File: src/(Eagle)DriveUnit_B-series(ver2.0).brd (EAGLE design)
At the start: 65.7 x 51 mm, 68 parts, among them IC1 A3921, SW1 TVAF06-A020B-R, SW2 TVAF06-A020B-R, SW3 THAF01-NC-R, SW4 SS-12D00G3

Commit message: 配線の追加
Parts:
- removed R28: 100k, GF063P B104K:GF063PB104K
- moved R12 0.20 mm to (49.2, 31.0)
- moved R10 0.17 mm to (49.2, 28.6)
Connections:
- removed net N$16: R13.RIGHT, R28.CENTER, R28.RIGHT
- net GND: now also R13.RIGHT; no longer R28.LEFT
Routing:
- net N$16: track 20.5 -> 0.00 mm, vias 2 -> 0
- net V5: track 23.1 -> 28.3 mm
- net VCC: track 0.00 -> 3.87 mm, vias 0 -> 2
- net GLB: track 10.2 -> 11.4 mm
- net GHB: track 7.57 -> 6.62 mm
- net N$4: track 6.13 -> 5.42 mm

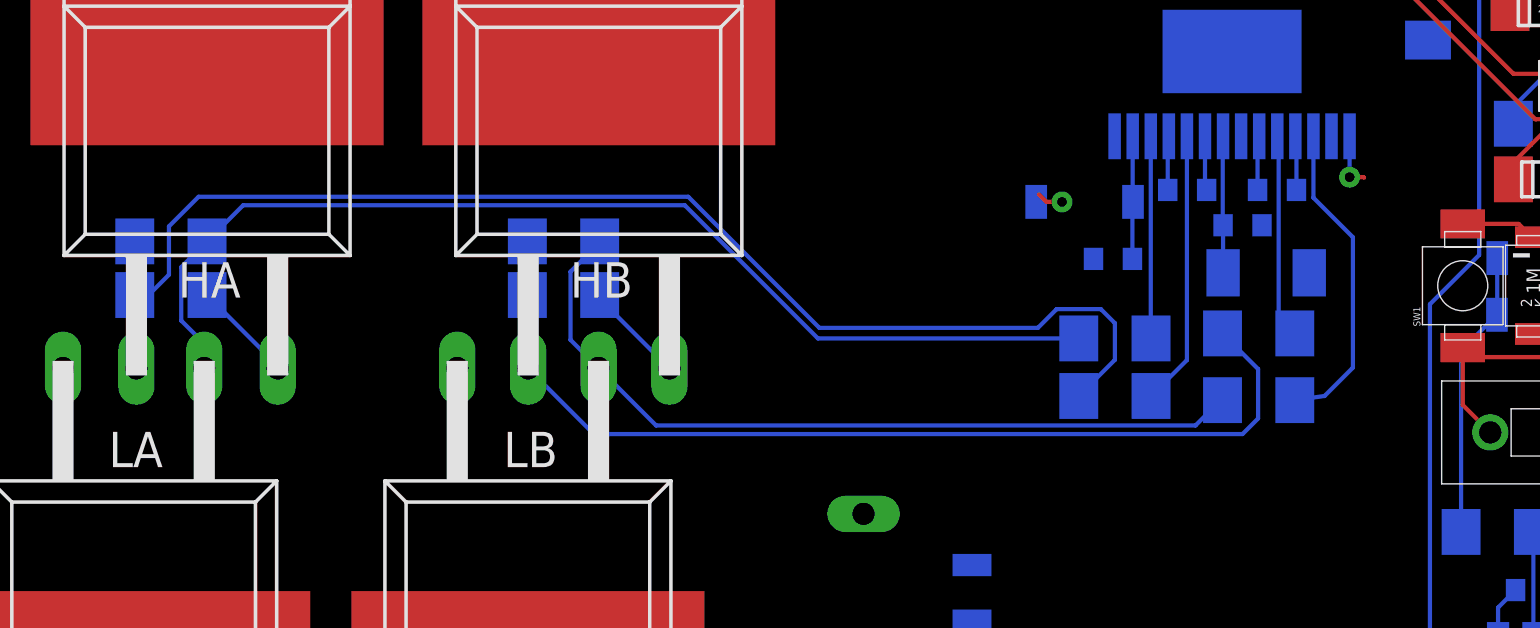
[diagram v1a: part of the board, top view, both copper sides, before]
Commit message: ビアなどの追加
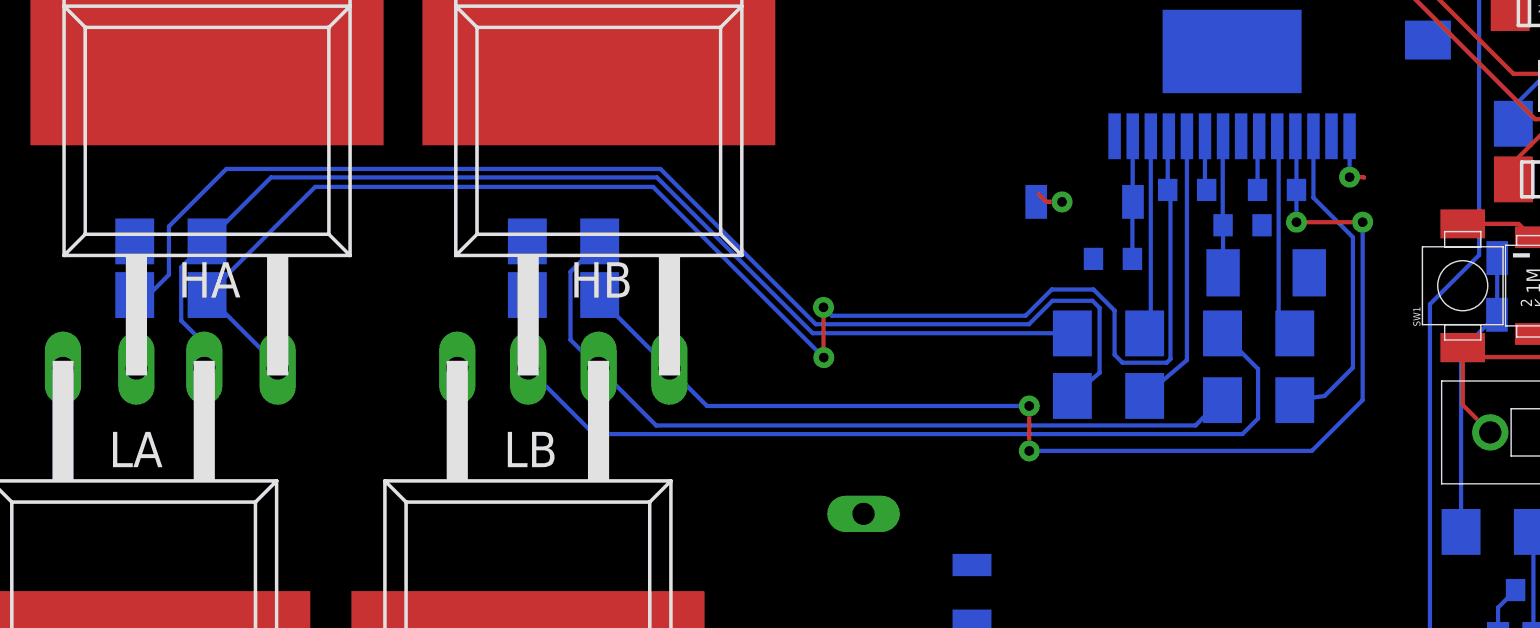
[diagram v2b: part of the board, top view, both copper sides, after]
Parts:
- moved R20 0.29 mm to (41.2, 31.0)
- moved R21 0.23 mm to (41.2, 28.8)
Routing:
- net SA: track 6.05 -> 55.4 mm, vias 0 -> 2
- net SB: track 10.8 -> 48.6 mm, vias 0 -> 4
- net N$13: track 43.3 -> 44.0 mm
- net N$25: track 39.2 -> 39.7 mm
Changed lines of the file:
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@@
 <attribute name="NAME" x="53.228" y="43.261" size="0.127" layer="26" rot="MR270"/>
 </element>
-<element name="R20" library="RG2012Q-100-D-T5" package="RG2012" value="RG2012Q-100-D-T5" x="41.43" y="30.82" smashed="yes" rot="MR180">
-<attribute name="NAME" x="42.446" y="30.058" size="0.127" layer="26" rot="MR180"/>
-</element>
-<element name="R21" library="RG2012Q-100-D-T5" package="RG2012" value="RG2012Q-100-D-T5" x="41.43" y="28.75" smashed="yes" rot="MR180">
-<attribute name="NAME" x="42.446" y="27.988" size="0.127" layer="26" rot="MR180"/>
+<element name="R20" library="RG2012Q-100-D-T5" package="RG2012" value="RG2012Q-100-D-T5" x="41.2" y="31" smashed="yes" rot="MR180">
+<attribute name="NAME" x="42.216" y="30.238" size="0.127" layer="26" rot="MR180"/>
+</element>
+<element name="R21" library="RG2012Q-100-D-T5" package="RG2012" value="RG2012Q-100-D-T5" x="41.2" y="28.75" smashed="yes" rot="MR180">
+<attribute name="NAME" x="42.216" y="27.988" size="0.127" layer="26" rot="MR180"/>
 </element>
 <element name="R22" library="RG2012P-681-B-T5" package="RG2012" value="RG2012P-681-B-T5" x="55.38" y="49.15" smashed="yes">
@@
 <wire x1="60.51" y1="38.7" x2="61.28" y2="38.54" width="0" layer="19" extent="1-16"/>
 <wire x1="64.21" y1="38.7" x2="62.31" y2="40.7" width="0" layer="19" extent="1-16"/>
+<wire x1="48.02" y1="34.89" x2="50.52" y2="38.09" width="0" layer="19" extent="16-16"/>
 <wire x1="51.15" y1="48.67" x2="44.66" y2="47.07" width="0" layer="19" extent="16-16"/>
 </signal>
@@
 <wire x1="24.2" y1="32.38" x2="24.2" y2="32.25" width="0.1524" layer="16"/>
 <wire x1="24.2" y1="32.25" x2="26.71" y2="29.74" width="0.1524" layer="16"/>
+<wire x1="49.26" y1="36.16" x2="49.26" y2="35" width="0.1524" layer="16"/>
+<via x="49.26" y="35" extent="1-16" drill="0.35"/>
+<wire x1="49.26" y1="35" x2="51.64" y2="35" width="0.1524" layer="1"/>
+<via x="51.64" y="35" extent="1-16" drill="0.35"/>
+<wire x1="51.64" y1="35" x2="51.64" y2="28.6017125" width="0.1524" layer="16"/>
+<wire x1="51.64" y1="28.6017125" x2="49.8134875" y2="26.7752" width="0.1524" layer="16"/>
+<wire x1="39.652" y1="26.7752" x2="39.65" y2="26.7732" width="0.1524" layer="16"/>
+<via x="39.65" y="26.7732" extent="1-16" drill="0.35"/>
+<wire x1="39.65" y1="26.7732" x2="39.65" y2="28.39" width="0.1524" layer="1"/>
+<via x="39.65" y="28.39" extent="1-16" drill="0.35"/>
+<wire x1="39.65" y1="28.39" x2="28.06" y2="28.39" width="0.1524" layer="16"/>
+<wire x1="28.06" y1="28.39" x2="26.71" y2="29.74" width="0.1524" layer="16"/>
+<wire x1="49.8134875" y1="26.7752" x2="39.652" y2="26.7752" width="0.1524" layer="16"/>
 <wire x1="49.22" y1="38.09" x2="59.69" y2="46.87" width="0" layer="19" extent="1-16"/>
-<wire x1="26.71" y1="29.74" x2="49.26" y2="36.16" width="0" layer="19" extent="16-16"/>
 <wire x1="21.62" y1="15.7646" x2="26.71" y2="29.74" width="0" layer="19" extent="1-1"/>
 <wire x1="22.68" y1="4.35" x2="21.62" y2="15.7646" width="0" layer="19" extent="1-1"/>
@@
 <wire x1="10.08" y1="32.38" x2="12.62" y2="29.84" width="0.1524" layer="16"/>
 <wire x1="12.62" y1="29.84" x2="12.62" y2="29.74" width="0.1524" layer="16"/>
+<wire x1="44.6268" y1="36.1568" x2="44.63" y2="36.16" width="0.1524" layer="16"/>
+<wire x1="44.5946875" y1="29.9464" x2="44.7286" y2="30.0803125" width="0.1524" layer="16"/>
+<wire x1="44.5946875" y1="29.9464" x2="43.0053125" y2="29.9464" width="0.1524" layer="16"/>
+<wire x1="42.72" y1="30.2317125" x2="42.72" y2="31.82" width="0.1524" layer="16"/>
+<wire x1="42.72" y1="31.82" x2="41.96" y2="32.58" width="0.1524" layer="16"/>
+<wire x1="40.46065625" y1="32.58" x2="39.51545625" y2="31.6348" width="0.1524" layer="16"/>
+<wire x1="39.51545625" y1="31.6348" x2="32.552" y2="31.6348" width="0.1524" layer="16"/>
+<wire x1="32.552" y1="31.6348" x2="32.25" y2="31.9368" width="0.1524" layer="16"/>
+<via x="32.25" y="31.9368" extent="1-16" drill="0.35"/>
+<wire x1="32.25" y1="31.9368" x2="32.25" y2="30.14" width="0.1524" layer="1"/>
+<wire x1="32.25" y1="30.14" x2="32.26" y2="30.13" width="0.1524" layer="1"/>
+<via x="32.26" y="30.13" extent="1-16" drill="0.35"/>
+<wire x1="32.26" y1="30.13" x2="26.12" y2="36.27" width="0.1524" layer="16"/>
+<wire x1="13.97" y1="36.27" x2="10.08" y2="32.38" width="0.1524" layer="16"/>
+<wire x1="43.0053125" y1="29.9464" x2="42.72" y2="30.2317125" width="0.1524" layer="16"/>
+<wire x1="41.96" y1="32.58" x2="40.46065625" y2="32.58" width="0.1524" layer="16"/>
+<wire x1="26.12" y1="36.27" x2="13.97" y2="36.27" width="0.1524" layer="16"/>
+<wire x1="44.7286" y1="30.0803125" x2="44.7286" y2="36.055" width="0.1524" layer="16"/>
+<wire x1="44.7286" y1="36.055" x2="44.6268" y2="36.1568" width="0.1524" layer="16"/>
 <wire x1="44.67" y1="38.09" x2="55" y2="47" width="0" layer="19" extent="1-16"/>
-<wire x1="12.62" y1="29.74" x2="44.63" y2="36.16" width="0" layer="19" extent="16-16"/>
 <wire x1="7.44" y1="15.7646" x2="12.62" y2="29.74" width="0" layer="19" extent="1-1"/>
 <wire x1="7.44" y1="4.35" x2="7.44" y2="15.7646" width="0" layer="19" extent="1-16"/>
@@
 <contactref element="R21" pad="RIGHT"/>
 <contactref element="IC1" pad="10"/>
-<wire x1="44.03" y1="28.75" x2="45.32" y2="30.04" width="0.1524" layer="16"/>
+<wire x1="43.8" y1="28.75" x2="45.32" y2="30.04" width="0.1524" layer="16"/>
 <wire x1="45.32" y1="30.04" x2="45.32" y2="38.09" width="0.1524" layer="16"/>
 </signal>
@@
 <contactref element="IC1" pad="12"/>
 <wire x1="44.02" y1="38.09" x2="44.02" y2="30.83" width="0.1524" layer="16"/>
-<wire x1="44.02" y1="30.83" x2="44.03" y2="30.82" width="0.1524" layer="16"/>
+<wire x1="44.02" y1="30.83" x2="43.8" y2="31" width="0.1524" layer="16"/>
 </signal>
 <signal name="N$2">
@@
 <wire x1="10.08" y1="34.31" x2="9.1514" y2="33.3814" width="0.1524" layer="16"/>
 <wire x1="9.1514" y1="33.3814" x2="9.1514" y2="31.4603125" width="0.1524" layer="16"/>
-<wire x1="41.43" y1="30.82" x2="32.05" y2="30.82" width="0.1524" layer="16"/>
-<wire x1="32.05" y1="30.82" x2="27.26" y2="35.61" width="0.1524" layer="16"/>
-<wire x1="27.26" y1="35.61" x2="11.38" y2="35.61" width="0.1524" layer="16"/>
-<wire x1="11.38" y1="35.61" x2="10.08" y2="34.31" width="0.1524" layer="16"/>
+<wire x1="26.26" y1="36.61" x2="31.8627" y2="31.0073" width="0.1524" layer="16"/>
+<wire x1="26.26" y1="36.61" x2="12.38" y2="36.61" width="0.1524" layer="16"/>
+<wire x1="12.38" y1="36.61" x2="10.08" y2="34.31" width="0.1524" layer="16"/>
+<wire x1="41.2" y1="31" x2="41.1927" y2="31.0073" width="0.1524" layer="16"/>
+<wire x1="41.1927" y1="31.0073" x2="31.8627" y2="31.0073" width="0.1524" layer="16"/>
 </signal>
 <signal name="N$26">
@@
 <contactref element="R16" pad="RIGHT"/>
 <contactref element="R21" pad="LEFT"/>
-<wire x1="41.43" y1="28.75" x2="42.73" y2="30.05" width="0.1524" layer="16"/>
-<wire x1="42.2246875" y1="31.8736" x2="40.6353125" y2="31.8736" width="0.1524" layer="16"/>
-<wire x1="40.6353125" y1="31.8736" x2="39.9617125" y2="31.2" width="0.1524" layer="16"/>
-<wire x1="42.73" y1="31.3682875" x2="42.2246875" y2="31.8736" width="0.1524" layer="16"/>
-<wire x1="32.10105625" y1="31.2" x2="27.38625625" y2="35.9148" width="0.1524" layer="16"/>
+<wire x1="41.2" y1="28.75" x2="42.18" y2="29.58268125" width="0.1524" layer="16"/>
+<wire x1="41.9246875" y1="32.1736" x2="40.4853125" y2="32.1736" width="0.1524" layer="16"/>
+<wire x1="40.4853125" y1="32.1736" x2="39.6417125" y2="31.33" width="0.1524" layer="16"/>
+<wire x1="42.18" y1="31.9182875" x2="41.9246875" y2="32.1736" width="0.1524" layer="16"/>
+<wire x1="31.97105625" y1="31.33" x2="26.38625625" y2="36.9148" width="0.1524" layer="16"/>
 <wire x1="8.71" y1="34.85" x2="8.71" y2="33.11" width="0.1524" layer="16"/>
 <wire x1="8.71" y1="33.11" x2="7.98" y2="32.38" width="0.1524" layer="16"/>
 <wire x1="7.98" y1="32.38" x2="7.48" y2="32.38" width="0.1524" layer="16"/>
-<wire x1="42.73" y1="30.05" x2="42.73" y2="31.3682875" width="0.1524" layer="16"/>
-<wire x1="39.9617125" y1="31.2" x2="32.10105625" y2="31.2" width="0.1524" layer="16"/>
-<wire x1="27.38625625" y1="35.9148" x2="9.7748" y2="35.9148" width="0.1524" layer="16"/>
-<wire x1="9.7748" y1="35.9148" x2="8.71" y2="34.85" width="0.1524" layer="16"/>
+<wire x1="42.18" y1="29.58268125" x2="42.18" y2="31.9182875" width="0.1524" layer="16"/>
+<wire x1="39.6417125" y1="31.33" x2="31.97105625" y2="31.33" width="0.1524" layer="16"/>
+<wire x1="26.38625625" y1="36.9148" x2="10.7748" y2="36.9148" width="0.1524" layer="16"/>
+<wire x1="10.7748" y1="36.9148" x2="8.71" y2="34.85" width="0.1524" layer="16"/>
 <wire x1="7.54" y1="29.74" x2="7.48" y2="32.38" width="0" layer="19" extent="16-16"/>
 </signal>

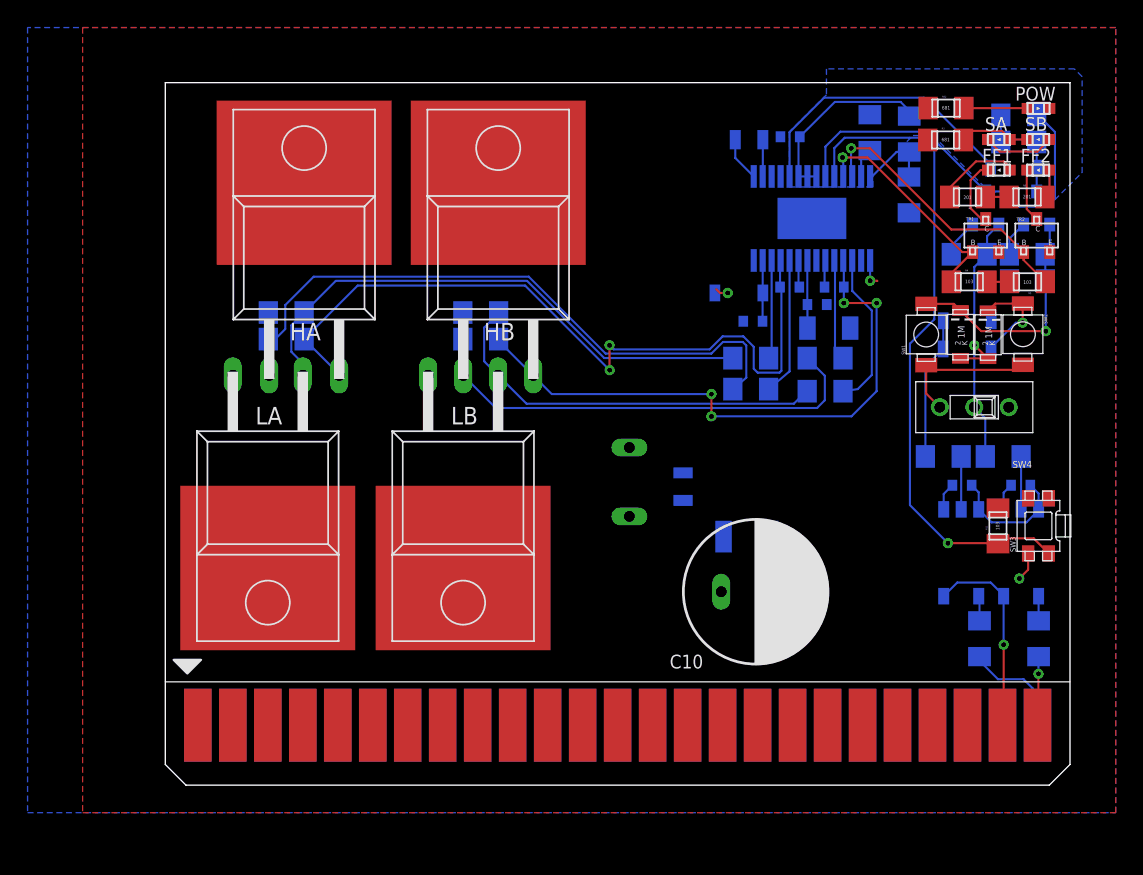
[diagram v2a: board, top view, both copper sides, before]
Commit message: SA，SBベタ以外は配線終了．
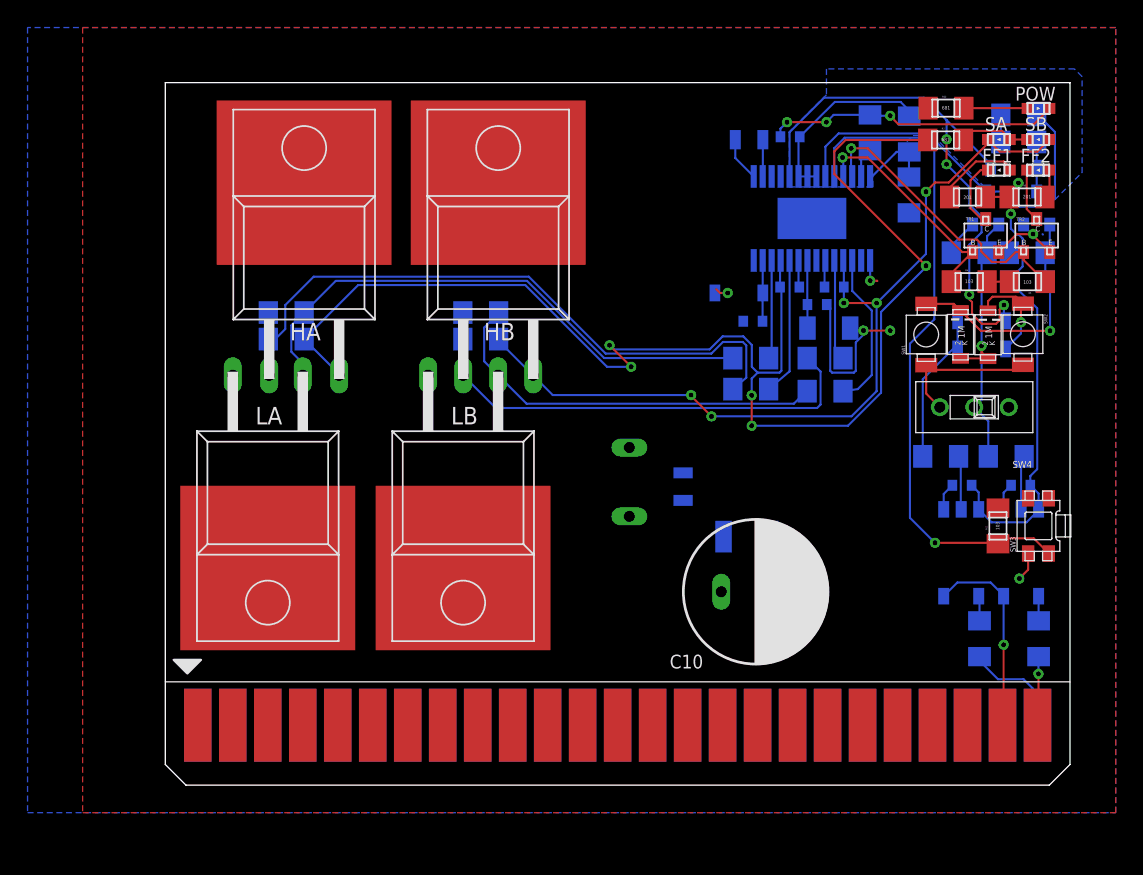
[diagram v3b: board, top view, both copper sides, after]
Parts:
- moved D6 1.05 mm to (61.0, 31.7)
- moved D2 1.04 mm to (61.0, 33.7)
- moved R9 0.22 mm to (59.8, 23.9)
- moved R1 0.19 mm to (55.0, 23.9)
- moved R24 0.11 mm to (63.9, 38.6)
- moved R25 0.11 mm to (59.7, 38.6)
- moved R17 0.08 mm to (63.9, 36.5)
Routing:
- net SA: track 55.4 -> 100.2 mm, vias 2 -> 5
- net GND: track 22.2 -> 58.5 mm, vias 1 -> 7
- net V5: track 28.3 -> 52.9 mm, vias 0 -> 2
- net DIR: track 21.1 -> 41.6 mm, vias 0 -> 4
- net SB: track 48.6 -> 63.5 mm, vias 4 -> 5
- net FF2: track 20.5 -> 21.4 mm
- net N$27: track 10.4 -> 11.2 mm
- net RESET: track 48.5 -> 49.1 mm

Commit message: 配線の終了
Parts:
- moved C12 7.31 mm to (35.9, 21.7), turned to 90 degrees
- moved C10 6.30 mm to (49.2, 14.0)
- moved C11 5.47 mm to (39.1, 21.1)
- moved C13 4.29 mm to (33.4, 22.5)
- moved LB 1.39 mm to (23.0, 24.6)
- moved HB 1.33 mm to (25.5, 34.7)
- moved R18 1.32 mm to (22.9, 34.3)
- moved R19 1.32 mm to (25.5, 32.4)
- moved LA 0.87 mm to (8.30, 24.6)
- moved R15 0.80 mm to (8.28, 34.3)
- moved R16 0.80 mm to (10.9, 32.4)
- moved HA 0.73 mm to (10.8, 34.7)
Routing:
- net V5: track 52.9 -> 56.0 mm
- net SB: track 63.5 -> 62.3 mm, vias 5 -> 69
- net N$21: track 33.4 -> 32.2 mm
- net N$26: track 29.2 -> 27.9 mm
- net SA: track 100.2 -> 99.4 mm, vias 5 -> 71
- net DIR: track 41.6 -> 42.3 mm
- net N$25: track 39.7 -> 39.0 mm
- net N$13: track 44.0 -> 43.4 mm
- added copper zone on layer 1, net SA
- added copper zone on layer 16, net SA
- added copper zone on layer 1, net SB
- added copper zone on layer 16, net SB
- added copper zone on layer 16, net VCC
